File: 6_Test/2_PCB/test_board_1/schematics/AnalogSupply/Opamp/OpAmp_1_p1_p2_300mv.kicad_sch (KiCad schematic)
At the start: 4 parts, among them U1 ADA4807-1AKSZ-R7

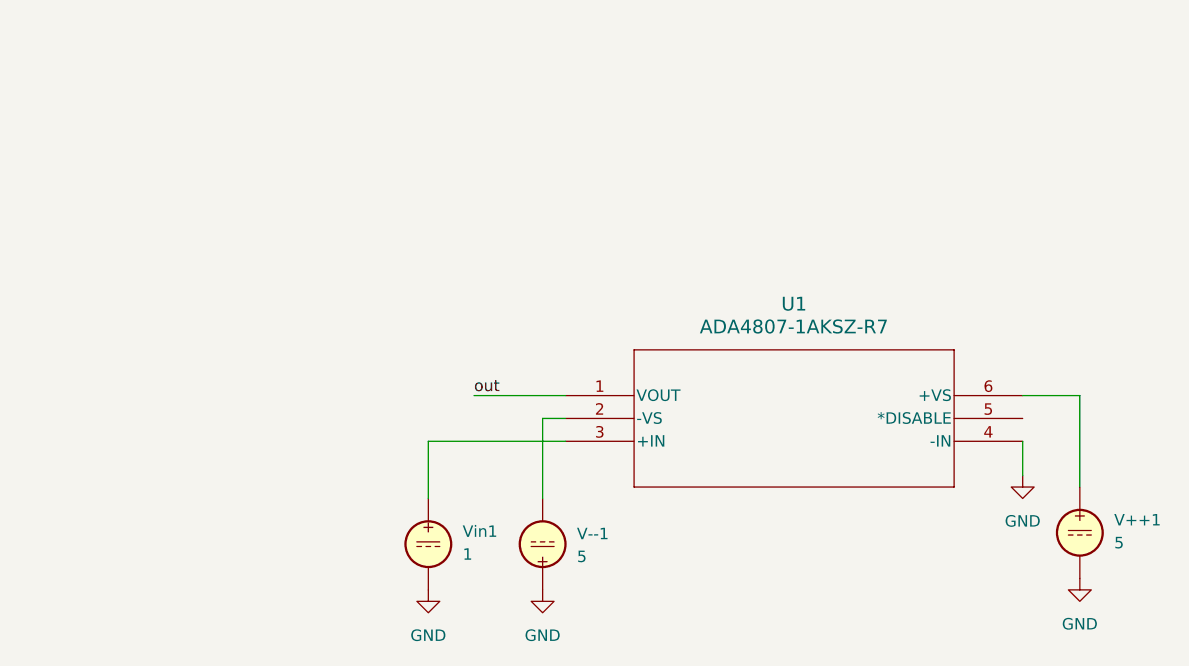
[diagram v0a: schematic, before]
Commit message: op amps done simulating
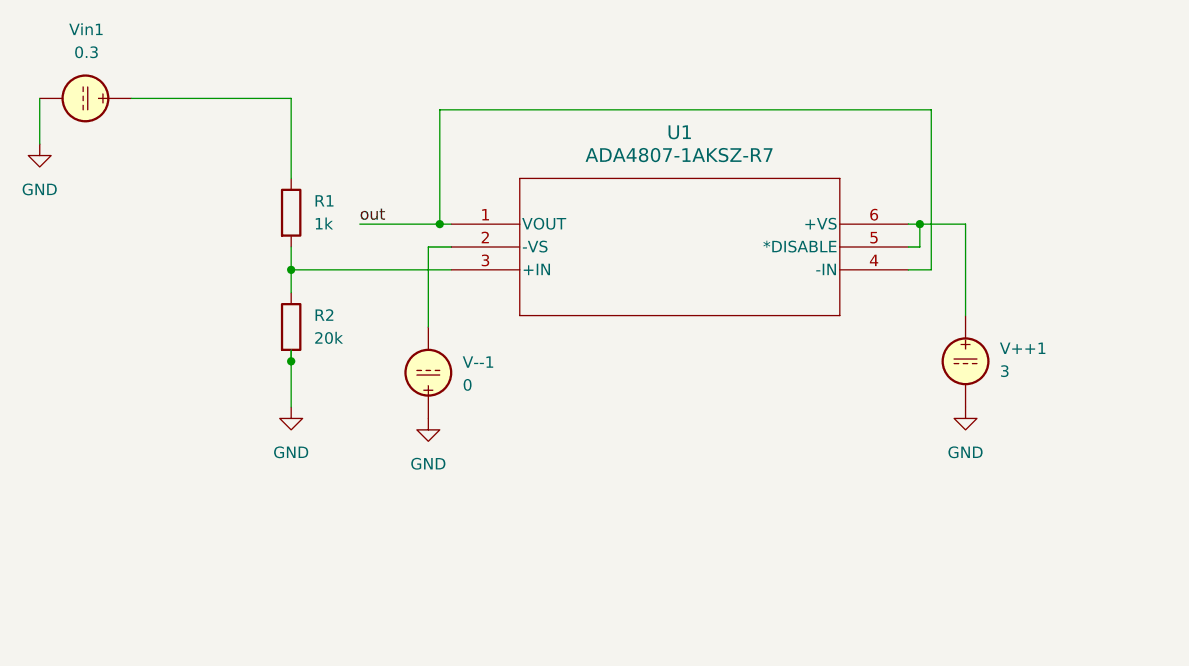
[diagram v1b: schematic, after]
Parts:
- added R1: 1k, symbol Device:R
- added R2: 20k, symbol Device:R
- V++1: value 5 -> 3
- V--1: value 5 -> 0
- Vin1: value 1 -> 0.3
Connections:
- net GND: now also R2.2; no longer U1.4 (-IN)
- net out: now also U1.4 (-IN)
- net at U1.6 (+VS), V++1.1: now also U1.5 (*DISABLE)
- net at U1.3 (+IN): now also R1.2, R2.1; no longer Vin1.1
- new net: R1.1, Vin1.1
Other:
- moved on the sheet: U1, V++1, V--1, Vin1
